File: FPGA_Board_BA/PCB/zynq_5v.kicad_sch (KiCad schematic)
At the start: 25 parts, among them U4 LM70860RRXR

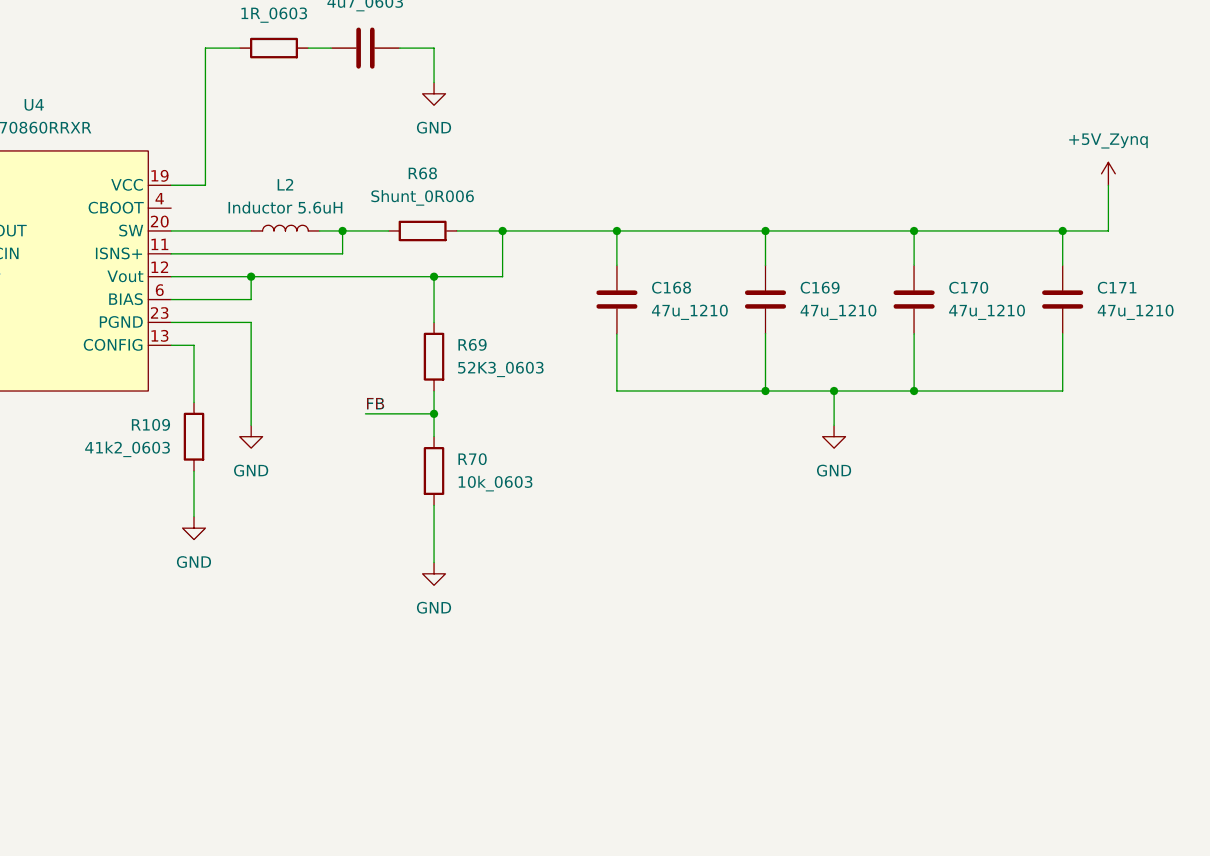
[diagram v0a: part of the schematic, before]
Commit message: layed out power supply for Zynq
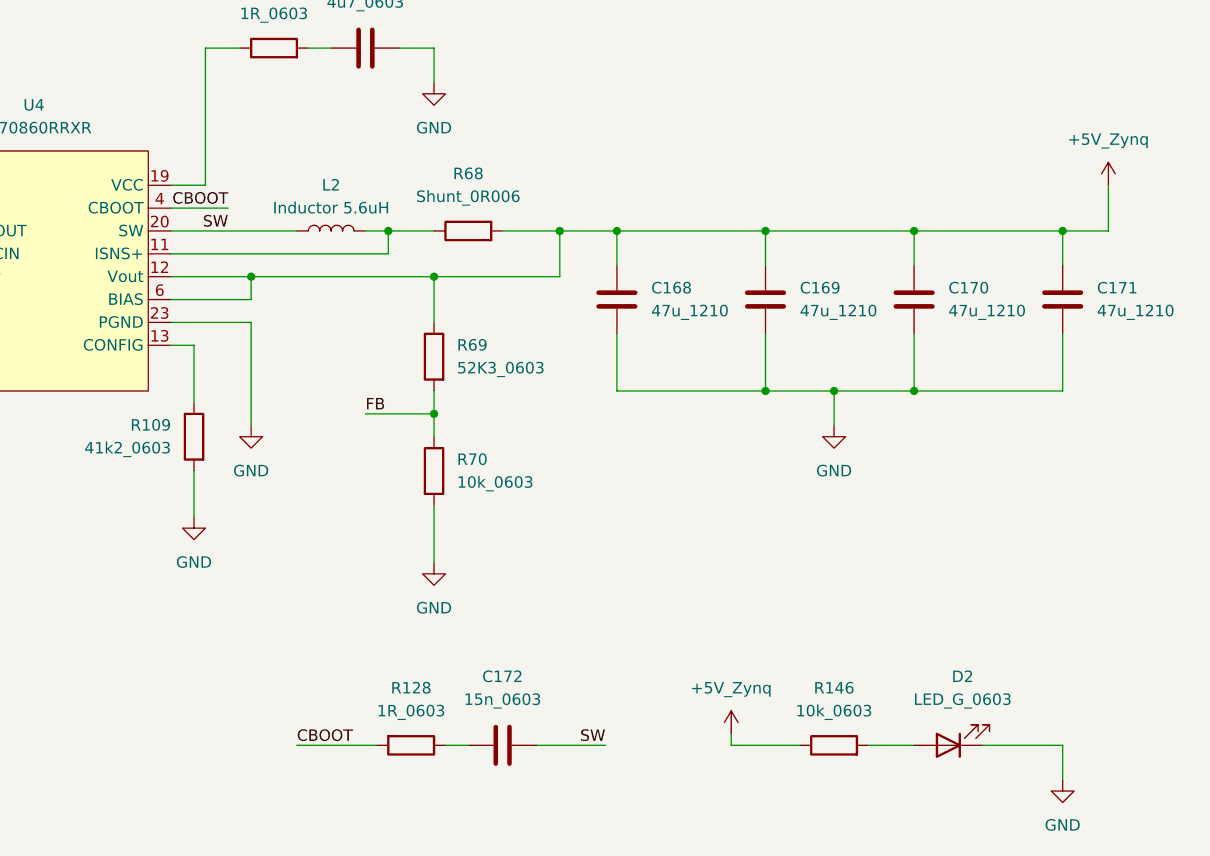
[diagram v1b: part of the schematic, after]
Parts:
- added C172: 15n_0603, WLIB_Capacitor:C_0603, symbol WLIB_C:15n_0603
- added D2: LED_G_0603, LED_SMD:LED_0603_1608Metric, symbol WLIB_D:LED_G_0603
- added R128: 1R_0603, Resistor_SMD:R_0603_1608Metric_Pad0.98x0.95mm_HandSolder, symbol WLIB_R:1R_0603
- added R146: 10k_0603, Resistor_SMD:R_0603_1608Metric, symbol WLIB_R:10k_0603
- C166, R127: footprint (none) -> Resistor_SMD:R_0603_1608Metric
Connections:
- net +5V_Zynq: now also R146.1
- net GND: now also U4.30 (PGND), D2.1 (K)
- net SW: now reaches L2.1, U4.20 (SW), U4.21 (SW), U4.22 (SW), U4.5 (SW)
- net SW: now also C172.2
- net CBOOT: now reaches U4.4 (CBOOT)
- net CBOOT: now also R128.2
- new net: D2.2 (A), R146.2
- new net: C172.1, R128.1
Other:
- moved on the sheet: L2, R68

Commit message: layout 99% ready
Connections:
- net SW: no longer names the net of L2.1, U4.20 (SW), U4.21 (SW), U4.22 (SW)
- net SW: no longer C172.2, U4.5 (SW)
- new net SW_Boot: C172.2, U4.5 (SW_Boot)
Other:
- moved on the sheet: C164, C165, C166, C167, C74, C75, C76, C77, R117, R118, R127, R71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

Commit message: layout ready to be reviewed by Leo
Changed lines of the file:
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@@
+	)
+	(junction
+		(at 274.32 87.63)
+		(diameter 0)
+		(color 0 0 0 0)
 	)
 	(junction
@@
 	(wire
 		(pts
+			(xy 274.32 87.63) (xy 278.13 87.63)
+		)
+		(stroke
+			(width 0)
+			(type default)
+		)
+	)
+	(wire
+		(pts
+			(xy 274.32 87.63) (xy 274.32 90.17)
+		)
+		(stroke
+			(width 0)
+			(type default)
+		)
+	)
+	(wire
+		(pts
 			(xy 139.7 87.63) (xy 99.06 87.63)
 		)
@@
 	(wire
 		(pts
-			(xy 274.32 85.09) (xy 274.32 90.17)
+			(xy 274.32 85.09) (xy 274.32 87.63)
 		)
 		(stroke
@@
 					(unit 1)
 				)
+			)
+		)
+	)
+	(symbol
+		(lib_id "power:PWR_FLAG")
+		(at 278.13 87.63 270)
+		(unit 1)
+		(exclude_from_sim no)
+		(in_bom yes)
+		(on_board yes)
+		(dnp no)
+		(fields_autoplaced yes)
+		(property "Reference" "#FLG05"
+			(at 280.035 87.63 0)
+			(effects
+				(font
+					(size 1.27 1.27)
+				)
+				(hide yes)
+			)
+		)
+		(property "Value" "PWR_FLAG"
+			(at 281.94 87.6299 90)
+			(effects
+				(font
+					(size 1.27 1.27)
+				)
+				(justify left)
+			)
+		)
+		(property "Footprint" ""
+			(at 278.13 87.63 0)
+			(effects
+				(font
+					(size 1.27 1.27)
+				)
+				(hide yes)
+			)
+		)
+		(property "Datasheet" "~"
+			(at 278.13 87.63 0)
+			(effects
+				(font
+					(size 1.27 1.27)
+				)
+				(hide yes)
+			)
+		)
+		(property "Description" "Special symbol for telling ERC where power comes from"
+			(at 278.13 87.63 0)
+			(effects
+				(font
+					(size 1.27 1.27)
+				)
+				(hide yes)
+			)
+		)
+		(pin "1"
+		)
+		(instances
+			(project ""
+				(path "/fd7503bc-e7fc-4766-b224-3d1c3d7de5ff/c218fce5-e0d6-44e0-8fcb-a1a13743da8a"
+					(reference "#FLG05")
+					(unit 1)
+				)
